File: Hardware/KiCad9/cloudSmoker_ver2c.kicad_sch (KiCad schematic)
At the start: 69 parts, among them J1 AudioJack2_SwitchT, J10 Conn_01x02_Pin, J11 Conn_01x02_Pin, J12 Conn_01x05, J13 Conn_01x08, J2 AudioJack2_SwitchT, J3 AudioJack2_SwitchT, J4 AudioJack2_SwitchT, J5 Conn_01x04_Pin, J6 Conn_01x04_Pin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

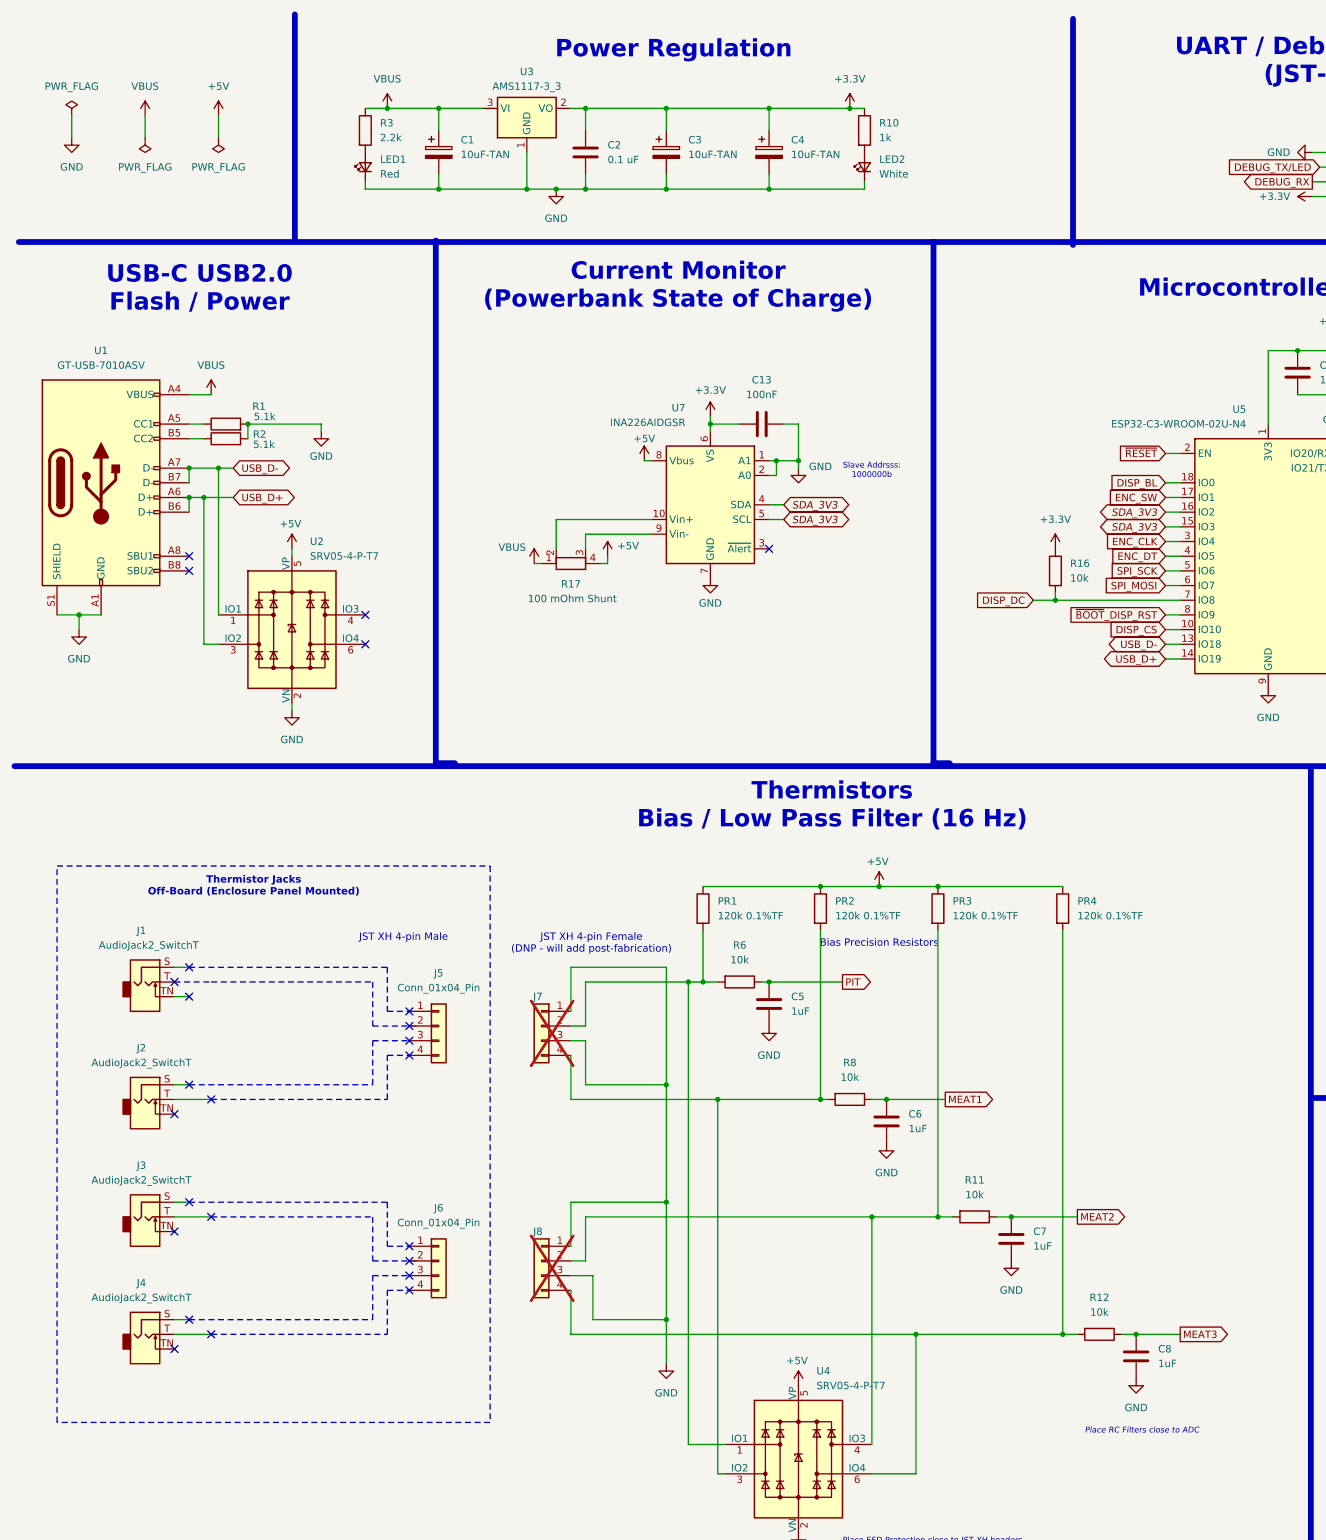
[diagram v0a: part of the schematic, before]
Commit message: create ver2C and archive ver2B as deprecated
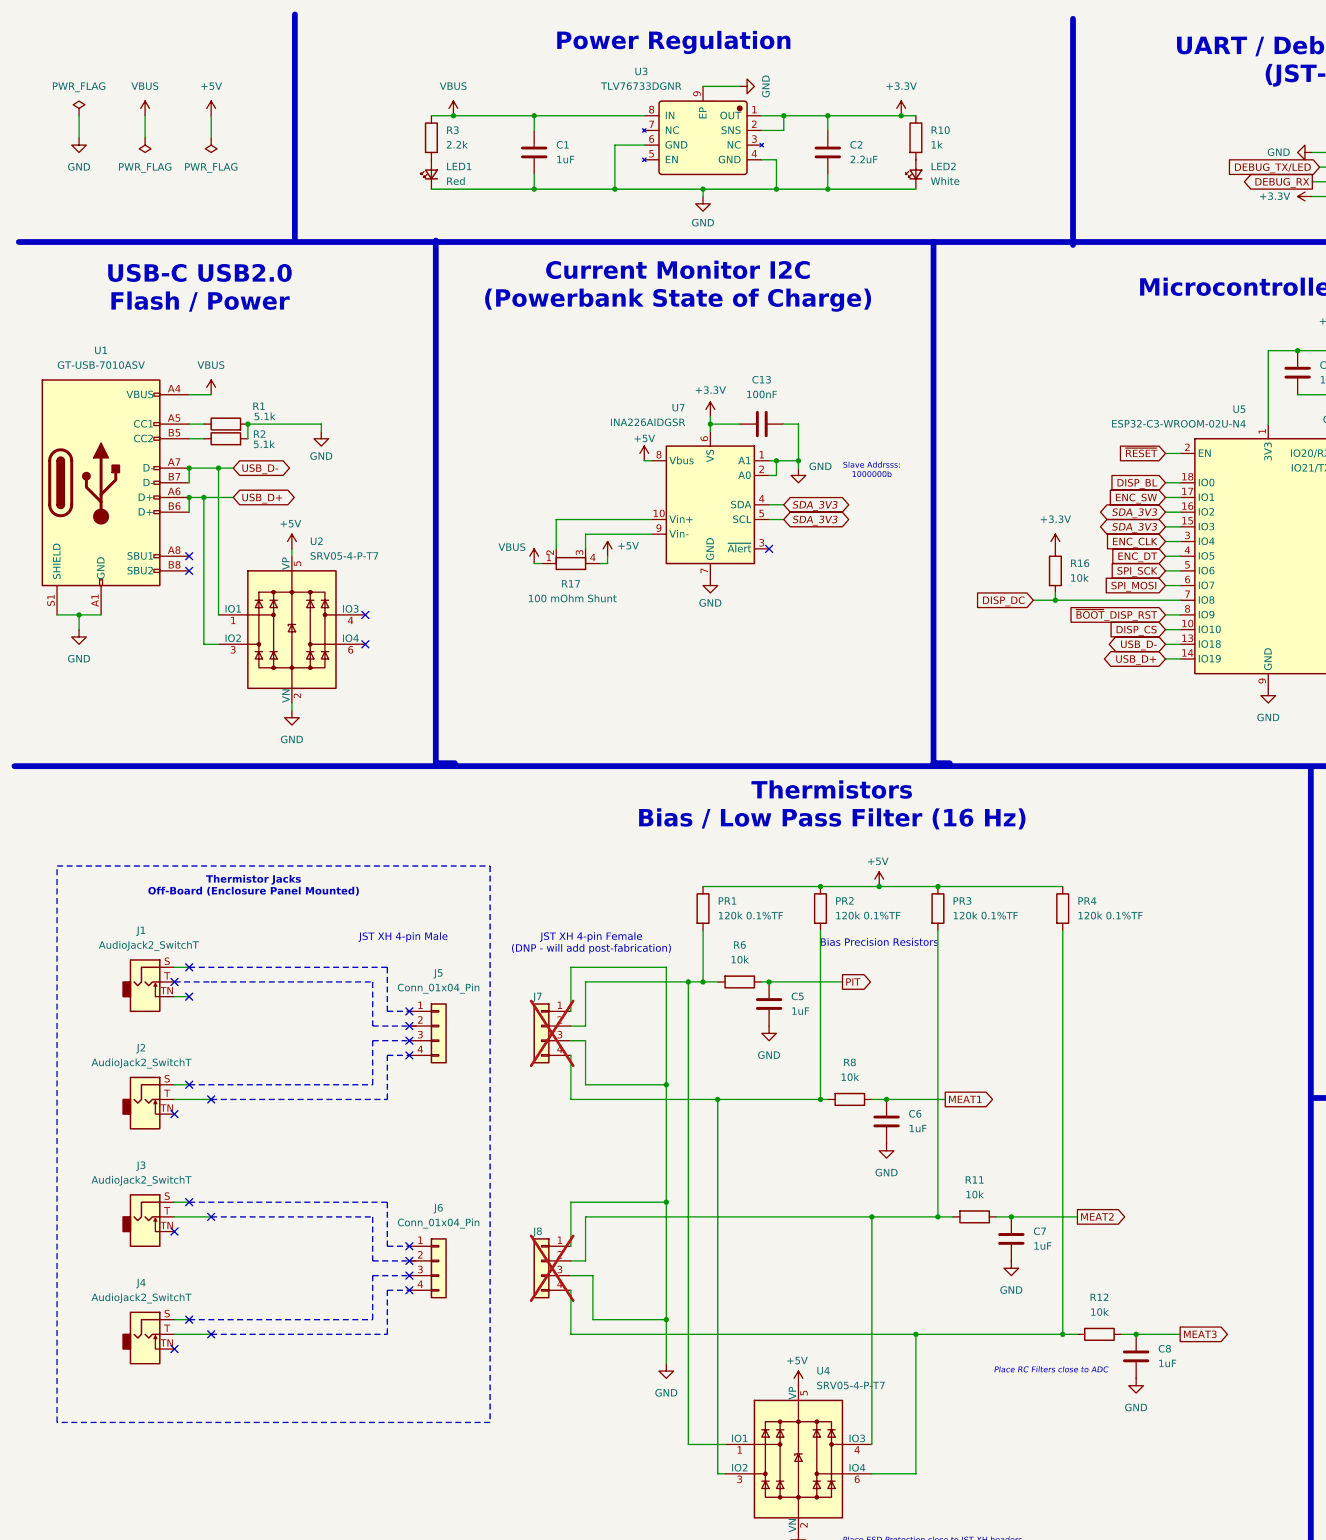
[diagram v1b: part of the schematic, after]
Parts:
- removed C1, C3, C4: 10uF-TAN, JLCImport:TAJA106K016RNJ, symbol Device:C_Polarized
- removed U3: AMS1117-3_3, Package_TO_SOT_SMD:SOT-223-3_TabPin2, symbol Regulator_Linear:AMS1117-3.3
- added C1: 1uF, JLCImport:CL10A105KB8NNNC, symbol Device:C
- added U3: TLV76733DGNR, JLCImport:TLV76733DGNR, symbol JLCImport:TLV76733DGNR
- C2: value 0.1 uF -> 2.2uF; footprint JLCImport:CC0603KRX7R9BB104 -> JLCImport:CL10A225KO8NNNC; LCSC C14663 -> C23630; Manufacturer YAGEO -> Samsung Electro-Mechanics; Manufacturer Part CC0603KRX7R9BB104 -> CL10A225KO8NNNC
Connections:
- net +3.3V: now also U3.1 (OUT), U3.2 (SNS)
- net GND: now also C1.2, U3.4 (GND), U3.6 (GND), U3.9 (EP)
- net VBUS: now also C1.1, U3.8 (IN)
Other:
- note added: "Current Monitor I2C (Powerbank State of Charge)"
- note removed: "Current Monitor (Powerbank State of Charge)"
- moved on the sheet: LED1, LED2, R10, R3
